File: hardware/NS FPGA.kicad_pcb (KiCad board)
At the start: 6 copper layers, 27.2 x 64.8 mm, 47 parts, among them J1 USB_C_Receptacle_USB2.0_14P, J2 Conn_01x24_Pin, J3 Conn_01x24_Pin, J4 Jtag PIN, Q1 BSS138, SW1 SW_Push, U2 CP2102N-Axx-xQFN24, U3 AP2112K-3.3, U4 AP2112K-1.2, Y1 SG-8002CE(24.0000M)

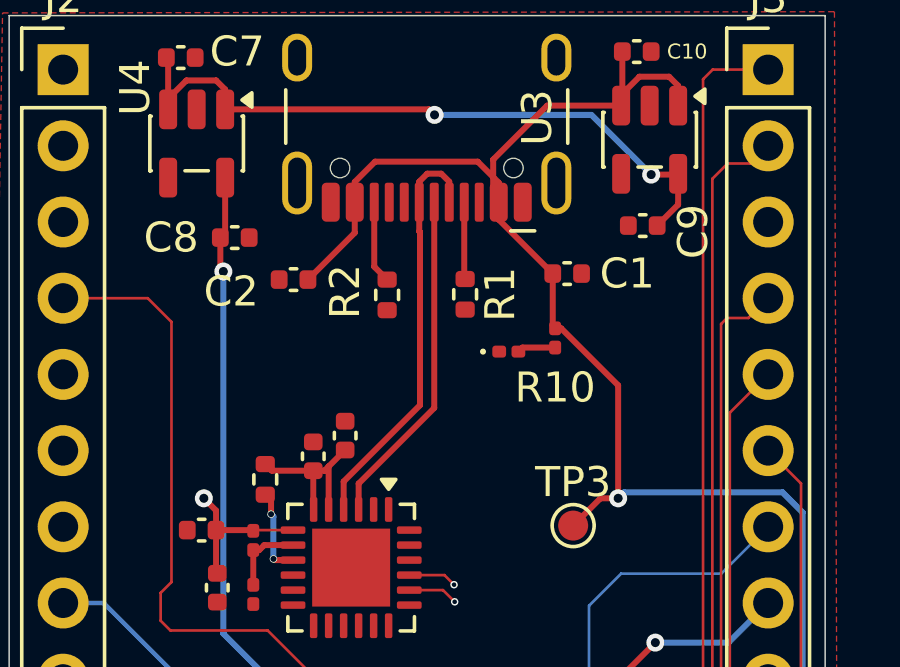
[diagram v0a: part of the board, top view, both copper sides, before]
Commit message: 1: fixed one of the differential trace by joining it with the other pad with a via. 2: Connected the floating ground pad with a trace to the body of the USB which is connected to the rest of the circuit.
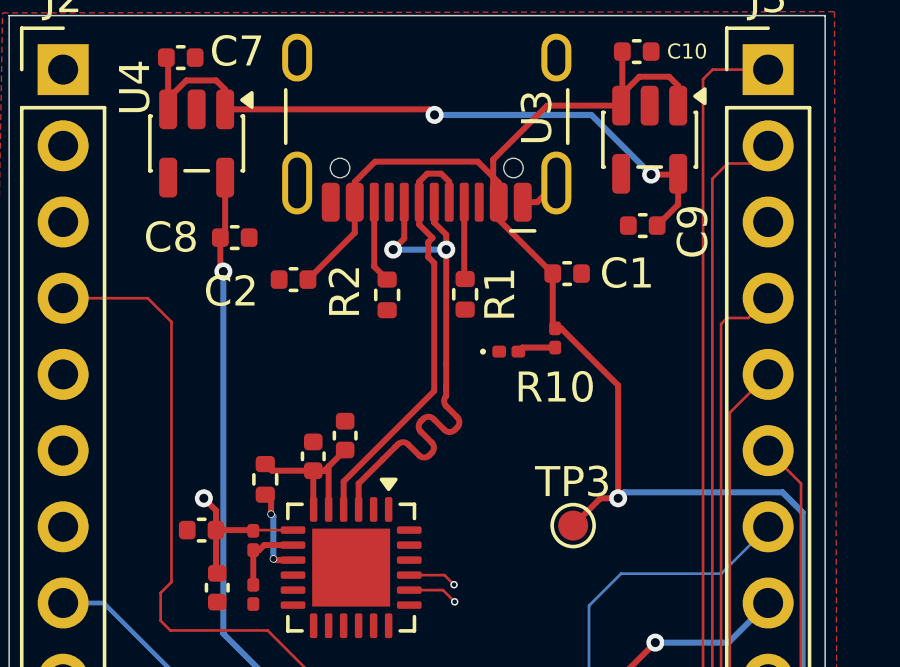
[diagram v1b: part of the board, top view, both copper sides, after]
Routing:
- net /D+: track 11.3 -> 18.2 mm, vias 0 -> 2
- net GND: track 37.5 -> 38.9 mm
- net /D-: track 13.9 -> 14.4 mm
